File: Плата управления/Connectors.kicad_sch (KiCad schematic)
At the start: 10 parts, among them J1 Conn_02x10_Odd_Even, J10 Conn_02x03_Odd_Even, J2 CAN2, J3 CAN1, J4 A, J5 B, J6 C, J7 RS485, J8 Conn_02x03_Odd_Even, J9 Conn_01x06

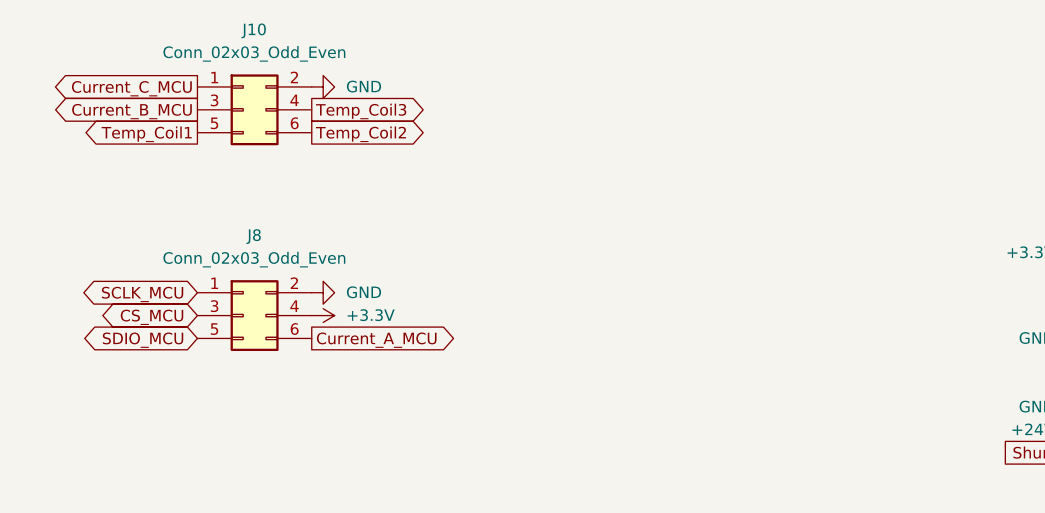
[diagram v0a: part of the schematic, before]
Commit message: Изменил межплатный разъем
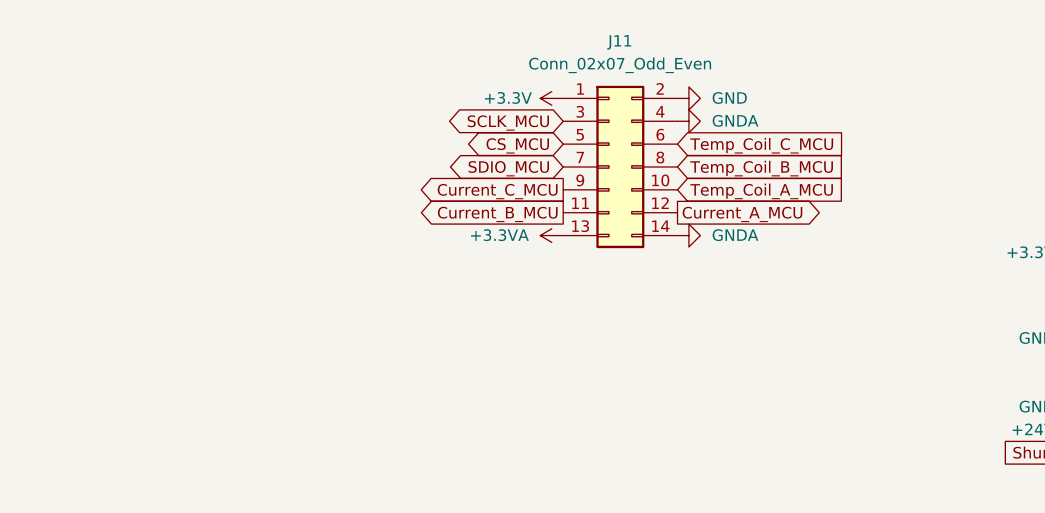
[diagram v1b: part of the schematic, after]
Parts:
- removed J10, J8: Conn_02x03_Odd_Even, Connector_PinHeader_2.54mm:PinHeader_2x03_P2.54mm_Vertical_SMD, symbol Connector_Generic:Conn_02x03_Odd_Even
- added J11: Conn_02x07_Odd_Even, Connector_PinHeader_2.54mm:PinHeader_2x07_P2.54mm_Vertical, symbol Connector_Generic:Conn_02x07_Odd_Even
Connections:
- net +3.3V: now also J11.1 (Pin_1)
- net CS_MCU: now also J11.5 (Pin_5)
- net Current_A_MCU: now also J11.12 (Pin_12)
- net Current_B_MCU: now also J11.11 (Pin_11)
- net Current_C_MCU: now also J11.9 (Pin_9)
- net GND: now also J11.2 (Pin_2)
- net GNDA: now also J11.14 (Pin_14), J11.4 (Pin_4)
- net SCLK_MCU: now also J11.3 (Pin_3)
- net SDIO_MCU: now also J11.7 (Pin_7)
- new net +3.3VA: J11.13 (Pin_13)
- new net Temp_Coil_A_MCU: J11.10 (Pin_10)
- new net Temp_Coil_B_MCU: J11.8 (Pin_8)
- new net Temp_Coil_C_MCU: J11.6 (Pin_6)

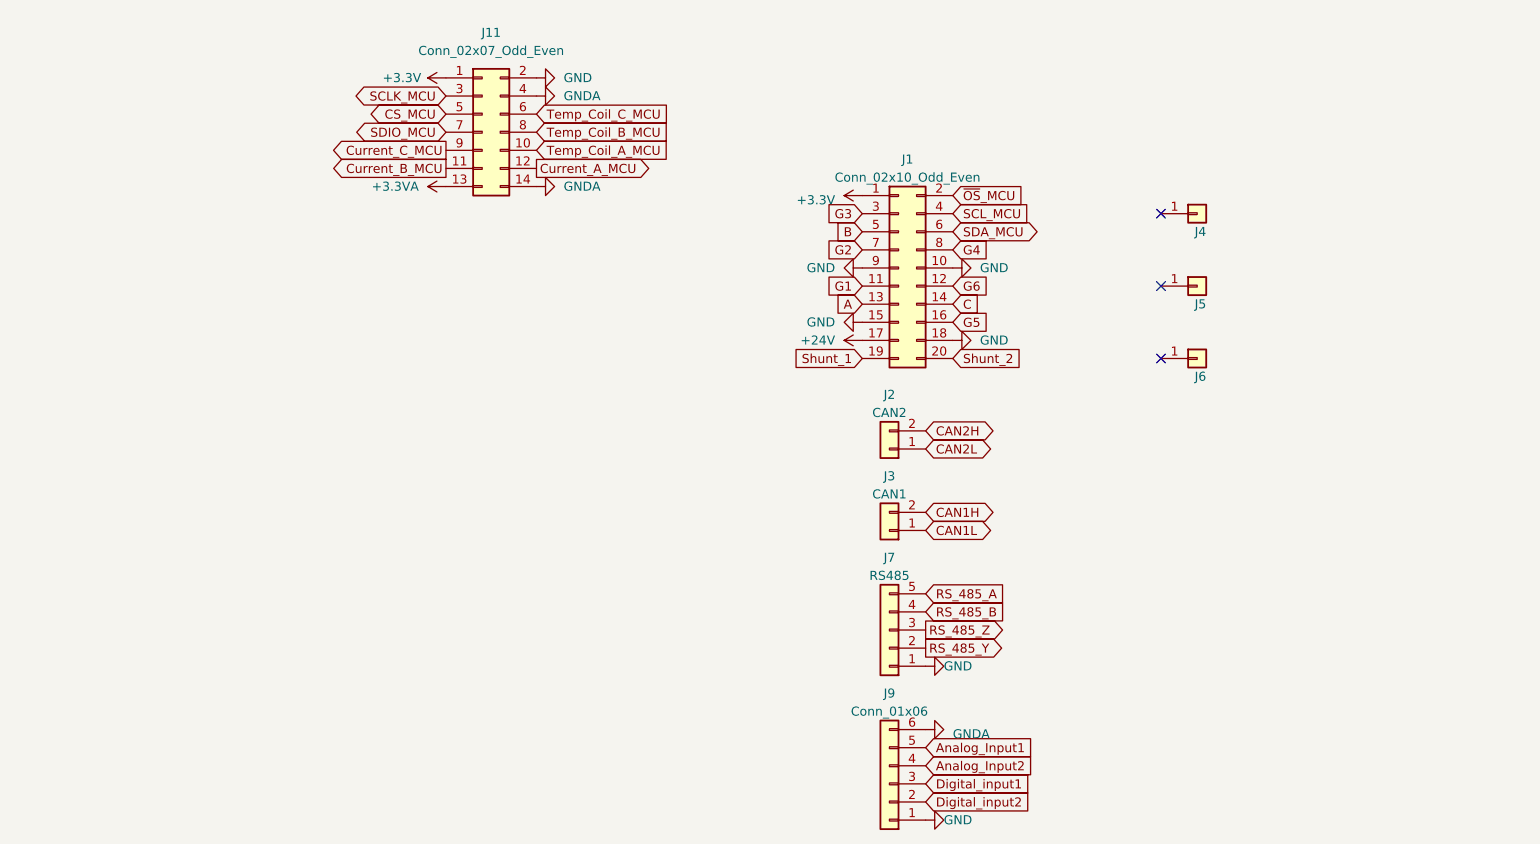
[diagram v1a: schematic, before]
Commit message: Разделил аналоговое и цифровое питание
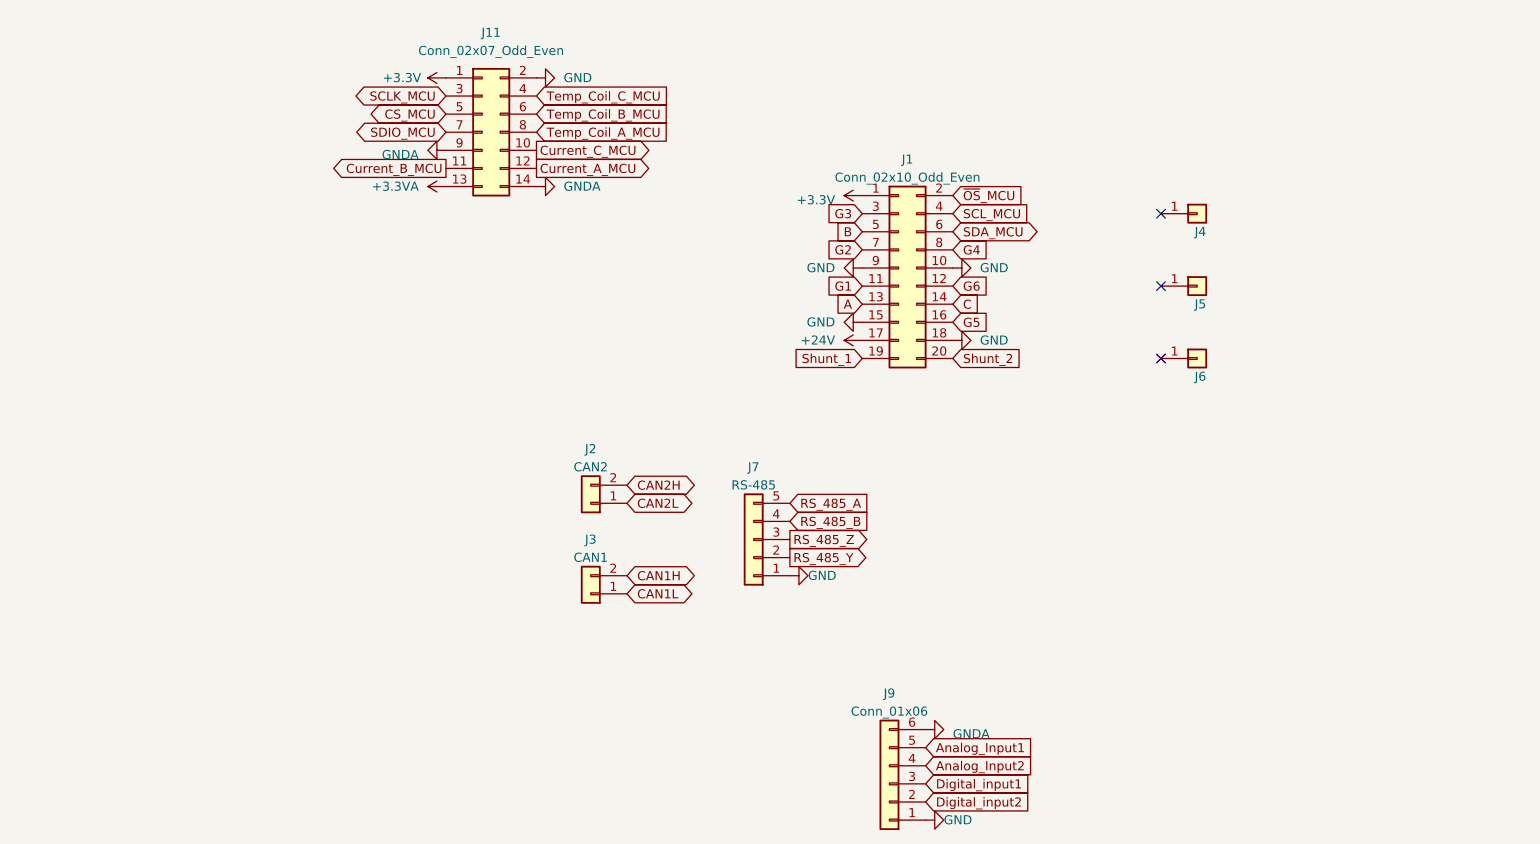
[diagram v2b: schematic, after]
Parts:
- J7: value RS485 -> RS-485
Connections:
- net Current_C_MCU: now also J11.10 (Pin_10); no longer J11.9 (Pin_9)
- net GNDA: now also J11.9 (Pin_9); no longer J11.4 (Pin_4)
- net Temp_Coil_A_MCU: now also J11.8 (Pin_8); no longer J11.10 (Pin_10)
- net Temp_Coil_B_MCU: now also J11.6 (Pin_6); no longer J11.8 (Pin_8)
- net Temp_Coil_C_MCU: now also J11.4 (Pin_4); no longer J11.6 (Pin_6)

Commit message: Редактировал схему
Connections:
- net CAN1H: now also J2.2 (Pin_2); no longer J3.2 (Pin_2)
- net CAN1L: now also J2.1 (Pin_1); no longer J3.1 (Pin_1)
- net CAN2H: now also J3.2 (Pin_2); no longer J2.2 (Pin_2)
- net CAN2L: now also J3.1 (Pin_1); no longer J2.1 (Pin_1)
- net CS_MCU renamed Angle_Sensor_SCLK_MCU
- net SCLK_MCU renamed Angle_Sensor_CS_MCU
- net SCL_MCU renamed Temperature_Power_SCL_MCU
- net SDA_MCU renamed Temperature_Power_SDA_MCU
- net SDIO_MCU renamed Angle_Sensor_SDIO_MCU
- net ~{OS}_MCU renamed Temperature_Power_~{OS}_MCU
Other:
- moved on the sheet: J4, J5, J6

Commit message: Ещё нужно доработать
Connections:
- net GNDA: no longer J11.9 (Pin_9)
- new net OUT_MCU: J11.9 (Pin_9)
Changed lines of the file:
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@@
+    )
+  )
+  (global_label "OUT_MCU" (shape output) (at 91.44 69.85 180) (fields_autoplaced)
+    (effects (font (size 1.27 1.27)) (justify right))
+    (property "Intersheetrefs" "${INTERSHEET_REFS}" (at 79.8861 69.85 0)
+      (effects (font (size 1.27 1.27)) (justify right) hide)
     )
   )
@@
         )
       )
-    )
-  )
-  (symbol (lib_id "power:GNDA") (at 91.44 69.85 270) (unit 1)
-    (in_bom yes) (on_board yes) (dnp no) (fields_autoplaced)
-    (property "Reference" "#PWR037" (at 85.09 69.85 0)
-      (effects (font (size 1.27 1.27)) hide)
-    )
-    (property "Value" "GNDA" (at 87.63 70.485 90)
-      (effects (font (size 1.27 1.27)) (justify right))
-    )
-    (property "Footprint" "" (at 91.44 69.85 0)
-      (effects (font (size 1.27 1.27)) hide)
-    )
-    (property "Datasheet" "" (at 91.44 69.85 0)
-      (effects (font (size 1.27 1.27)) hide)
-    )
-    (pin "1")
-    (instances
-      (project "Плата управления"
-        (path "/75f4c67c-bbde-4446-8f82-67797a1b269f/f5e732cc-be4b-4207-bf28-0691ff32221d"
-          (reference "#PWR037") (unit 1)
-        )
-      )

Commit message: Добавил документы
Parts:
- J9: value Conn_01x06 -> Inputs
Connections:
- net Analog_Input2 is gone; now on net +3.3VA: J9.4 (Pin_4)
- net Digital_input2 is gone; now on net +3.3V: J9.2 (Pin_2)
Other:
- note added: "Наружний разъём"
- note added: "Разъём платы датчиков"
- note added: "Разъём платы силовой"
- note added: "Фазные разъёмы"
- moved on the sheet: J1, J11, J2, J3, J4, J5, J6, J7, J9

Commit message: Добавил все документы
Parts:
- renumbered J4 to J1, J5 to J2, J6 to J3, J2 to J4, J11 to J5, J3 to J6, J1 to J8

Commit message: Версия под отчёт
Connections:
- net +3.3V: no longer J9.2 (Pin_2)
- net +3.3VA: no longer J9.4 (Pin_4)
- new net Analog_Input2: J9.4 (Pin_4)
- new net Digital_input2: J9.2 (Pin_2)
- no-connect marks 3 -> 0
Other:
- moved on the sheet: J1, J2, J3
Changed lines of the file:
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@@
     (comment 1 "МПСТ.76721.758764.02.Э3.М")
   )
-  (no_connect (at 210.82 86.995))
-  (no_connect (at 220.98 86.995))
-  (no_connect (at 200.66 86.995))
   (rectangle (start 126.365 107.315) (end 189.23 146.685)
     (stroke (width 0) (type dash))
     (fill (type none))
   )
-  (rectangle (start 230.505 73.025) (end 193.04 93.98)
+  (rectangle (start 74.93 75.565) (end 37.465 96.52)
     (stroke (width 0) (type dash))
     (fill (type none))
@@
     (fill (type none))
   )
-  (text "Фазные разъёмы" (at 198.755 71.755 0)
-    (effects (font (size 2 2) (thickness 0.4) bold) (justify left bottom))
+  (text "Фазные разъёмы" (at 43.18 74.295 0)
+    (effects (font (size 2.5 2.5) (thickness 0.4) bold) (justify left bottom))
   )
   (text "Разъём платы датчиков\n" (at 139.065 71.755 0)
-    (effects (font (size 2 2) (thickness 0.4) bold) (justify left bottom))
+    (effects (font (size 2.5 2.5) (thickness 0.4) bold) (justify left bottom))
   )
   (text "Наружний разъём\n" (at 84.455 74.295 0)
-    (effects (font (size 2 2) (thickness 0.4) bold) (justify left bottom))
-  )
-  (text "Разъём платы силовой\n" (at 140.335 106.045 0)
-    (effects (font (size 2 2) (thickness 0.4) bold) (justify left bottom))
+    (effects (font (size 2.5 2.5) (thickness 0.4) bold) (justify left bottom))
+  )
+  (text "Разъём платы силовой\n" (at 144.145 106.68 0)
+    (effects (font (size 2.5 2.5) (thickness 0.4) bold) (justify left bottom))
   )
   (global_label "G3" (shape input) (at 141.605 118.11 180) (fields_autoplaced)
@@
     )
   )
+  (global_label "Digital_input1" (shape input) (at 95.25 132.715 0) (fields_autoplaced)
+    (effects (font (size 1.27 1.27)) (justify left))
+    (property "Intersheetrefs" "${INTERSHEET_REFS}" (at 111.3583 132.715 0)
+      (effects (font (size 1.27 1.27)) (justify left) hide)
+    )
+  )
   (global_label "Temp_Coil_A_MCU" (shape input) (at 168.275 88.9 0) (fields_autoplaced)
     (effects (font (size 1.27 1.27)) (justify left))
@@
     )
   )
+  (global_label "Analog_Input2" (shape input) (at 95.25 130.175 0) (fields_autoplaced)
+    (effects (font (size 1.27 1.27)) (justify left))
+    (property "Intersheetrefs" "${INTERSHEET_REFS}" (at 109.0703 130.175 0)
+      (effects (font (size 1.27 1.27)) (justify left) hide)
+    )
+  )
   (global_label "OUT_MCU" (shape output) (at 155.575 91.44 180) (fields_autoplaced)
     (effects (font (size 1.27 1.27)) (justify right))
@@
     )
   )
-  (global_label "Digital_input1" (shape input) (at 95.25 132.715 0) (fields_autoplaced)
-    (effects (font (size 1.27 1.27)) (justify left))
-    (property "Intersheetrefs" "${INTERSHEET_REFS}" (at 111.3583 132.715 0)
+  (global_label "Digital_input2" (shape input) (at 95.25 135.255 0) (fields_autoplaced)
+    (effects (font (size 1.27 1.27)) (justify left))
+    (property "Intersheetrefs" "${INTERSHEET_REFS}" (at 108.6894 135.255 0)
       (effects (font (size 1.27 1.27)) (justify left) hide)
     )
@@
         (path "/75f4c67c-bbde-4446-8f82-67797a1b269f/f5e732cc-be4b-4207-bf28-0691ff32221d"
           (reference "#PWR031") (unit 1)
-        )
-      )
-      (project "Силовая плата"
-        (path "/96c6fc92-8ec6-44f7-b0dc-9ad8f1acea09/a27b443f-c036-4fd6-934c-6ea912709de0"
-          (reference "#PWR042") (unit 1)
-        )
-      )
-    )
-  )
-  (symbol (lib_id "power:+3.3V") (at 95.25 135.255 270) (unit 1)
-    (in_bom yes) (on_board yes) (dnp no)
-    (property "Reference" "#PWR038" (at 91.44 135.255 0)
-      (effects (font (size 1.27 1.27)) hide)
-    )
-    (property "Value" "+3.3V" (at 97.79 135.255 90)
-      (effects (font (size 1.27 1.27)) (justify left))
-    )
-    (property "Footprint" "" (at 95.25 135.255 0)
-      (effects (font (size 1.27 1.27)) hide)
-    )
-    (property "Datasheet" "" (at 95.25 135.255 0)
-      (effects (font (size 1.27 1.27)) hide)
-    )
-    (pin "1")
-    (instances
-      (project "Плата управления"
-        (path "/75f4c67c-bbde-4446-8f82-67797a1b269f/f5e732cc-be4b-4207-bf28-0691ff32221d"
-          (reference "#PWR038") (unit 1)
         )
       )
@@
     )
   )
-  (symbol (lib_id "Connector_Generic:Conn_01x01") (at 210.82 81.915 90) (unit 1)
+  (symbol (lib_id "Connector_Generic:Conn_01x01") (at 55.245 84.455 90) (unit 1)
     (in_bom yes) (on_board yes) (dnp no)
-    (property "Reference" "J2" (at 213.36 80.645 0)
+    (property "Reference" "J2" (at 54.61 81.915 90)
       (effects (font (size 1.27 1.27)) (justify right))
     )
-    (property "Value" "B" (at 213.36 83.185 90)
-      (effects (font (size 1.27 1.27)) (justify right) hide)
-    )
-    (property "Footprint" "Connector_My:Power_Wire" (at 210.82 81.915 0)
-      (effects (font (size 1.27 1.27)) hide)
-    )
-    (property "Datasheet" "~" (at 210.82 81.915 0)
+    (property "Value" "B" (at 57.785 85.725 90)
+      (effects (font (size 1.27 1.27)) (justify right) hide)
+    )
+    (property "Footprint" "Connector_My:Power_Wire" (at 55.245 84.455 0)
+      (effects (font (size 1.27 1.27)) hide)
+    )
+    (property "Datasheet" "~" (at 55.245 84.455 0)
       (effects (font (size 1.27 1.27)) hide)
     )
@@
     )
   )
-  (symbol (lib_id "Connector_Generic:Conn_01x01") (at 220.98 81.915 90) (unit 1)
+  (symbol (lib_id "Connector_Generic:Conn_01x01") (at 65.405 84.455 90) (unit 1)
     (in_bom yes) (on_board yes) (dnp no)
-    (property "Reference" "J3" (at 223.52 80.645 0)
+    (property "Reference" "J3" (at 64.77 81.915 90)
       (effects (font (size 1.27 1.27)) (justify right))
     )
-    (property "Value" "C" (at 223.52 83.185 90)
-      (effects (font (size 1.27 1.27)) (justify right) hide)
-    )
-    (property "Footprint" "Connector_My:Power_Wire" (at 220.98 81.915 0)
-      (effects (font (size 1.27 1.27)) hide)
-    )
-    (property "Datasheet" "~" (at 220.98 81.915 0)
+    (property "Value" "C" (at 67.945 85.725 90)
+      (effects (font (size 1.27 1.27)) (justify right) hide)
+    )
+    (property "Footprint" "Connector_My:Power_Wire" (at 65.405 84.455 0)
+      (effects (font (size 1.27 1.27)) hide)
+    )
+    (property "Datasheet" "~" (at 65.405 84.455 0)
       (effects (font (size 1.27 1.27)) hide)
     )
@@
     )
   )
-  (symbol (lib_id "Connector_Generic:Conn_01x01") (at 200.66 81.915 90) (unit 1)
+  (symbol (lib_id "Connector_Generic:Conn_01x01") (at 45.085 84.455 90) (unit 1)
     (in_bom yes) (on_board yes) (dnp no)
-    (property "Reference" "J1" (at 203.2 80.645 0)
+    (property "Reference" "J1" (at 44.45 81.915 90)
       (effects (font (size 1.27 1.27)) (justify right))
     )
-    (property "Value" "A" (at 203.2 83.185 90)
-      (effects (font (size 1.27 1.27)) (justify right) hide)
-    )
-    (property "Footprint" "Connector_My:Power_Wire" (at 200.66 81.915 0)
-      (effects (font (size 1.27 1.27)) hide)
-    )
-    (property "Datasheet" "~" (at 200.66 81.915 0)
+    (property "Value" "A" (at 47.625 85.725 90)
+      (effects (font (size 1.27 1.27)) (justify right) hide)
+    )
+    (property "Footprint" "Connector_My:Power_Wire" (at 45.085 84.455 0)
+      (effects (font (size 1.27 1.27)) hide)
+    )
+    (property "Datasheet" "~" (at 45.085 84.455 0)
       (effects (font (size 1.27 1.27)) hide)
     )
@@
         )
       )
-    )
-  )
-  (symbol (lib_id "power:+3.3VA") (at 95.25 130.175 270) (unit 1)
-    (in_bom yes) (on_board yes) (dnp no)
-    (property "Reference" "#PWR036" (at 91.44 130.175 0)
-      (effects (font (size 1.27 1.27)) hide)
-    )
-    (property "Value" "+3.3VA" (at 97.79 130.175 90)
-      (effects (font (size 1.27 1.27)) (justify left))
-    )
-    (property "Footprint" "" (at 95.25 130.175 0)
-      (effects (font (size 1.27 1.27)) hide)
-    )
-    (property "Datasheet" "" (at 95.25 130.175 0)
-      (effects (font (size 1.27 1.27)) hide)
-    )
-    (pin "1")
-    (instances
-      (project "Плата управления"
-        (path "/75f4c67c-bbde-4446-8f82-67797a1b269f/f5e732cc-be4b-4207-bf28-0691ff32221d"
-          (reference "#PWR036") (unit 1)
-        )
-      )

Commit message: Версия в производство 1.0
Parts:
- J4: value CAN2 -> CAN1
- J6: value CAN1 -> CAN2
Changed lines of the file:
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@@
   (paper "A4")
   (title_block
-    (comment 1 "МПСТ.76721.758764.02.Э3.М")
+    (comment 1 "МПСТ.76721.758764.02.М Э3")
   )
   (rectangle (start 126.365 107.315) (end 189.23 146.685)
@@
       (effects (font (size 1.27 1.27)))
     )
-    (property "Value" "CAN1" (at 87.63 99.06 90)
+    (property "Value" "CAN2" (at 87.63 99.06 90)
       (effects (font (size 1.27 1.27)))
     )
@@
       (effects (font (size 1.27 1.27)))
     )
-    (property "Value" "CAN2" (at 87.63 86.36 90)
+    (property "Value" "CAN1" (at 87.63 86.36 90)
       (effects (font (size 1.27 1.27)))
     )
